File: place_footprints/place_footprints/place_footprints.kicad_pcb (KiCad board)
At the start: 2 copper layers, 64 parts

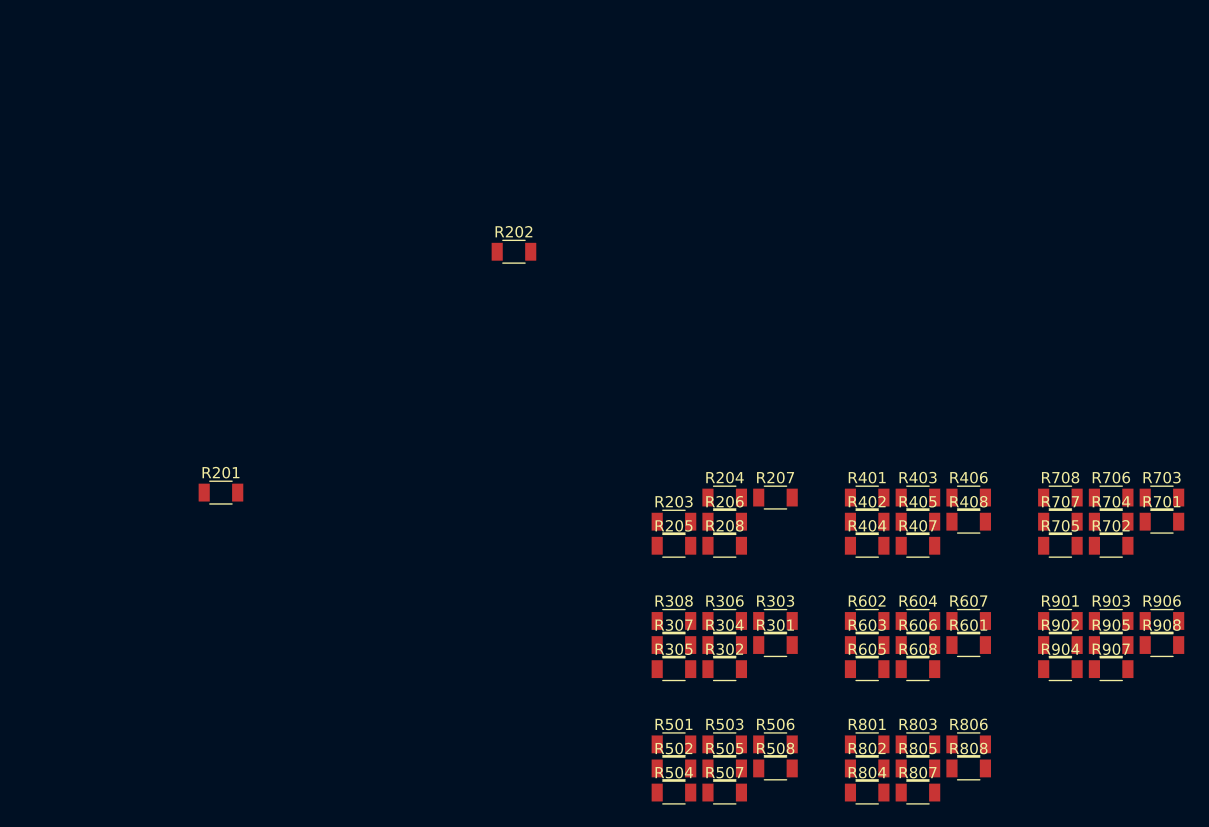
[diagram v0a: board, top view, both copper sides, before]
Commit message: Fixed circular placement
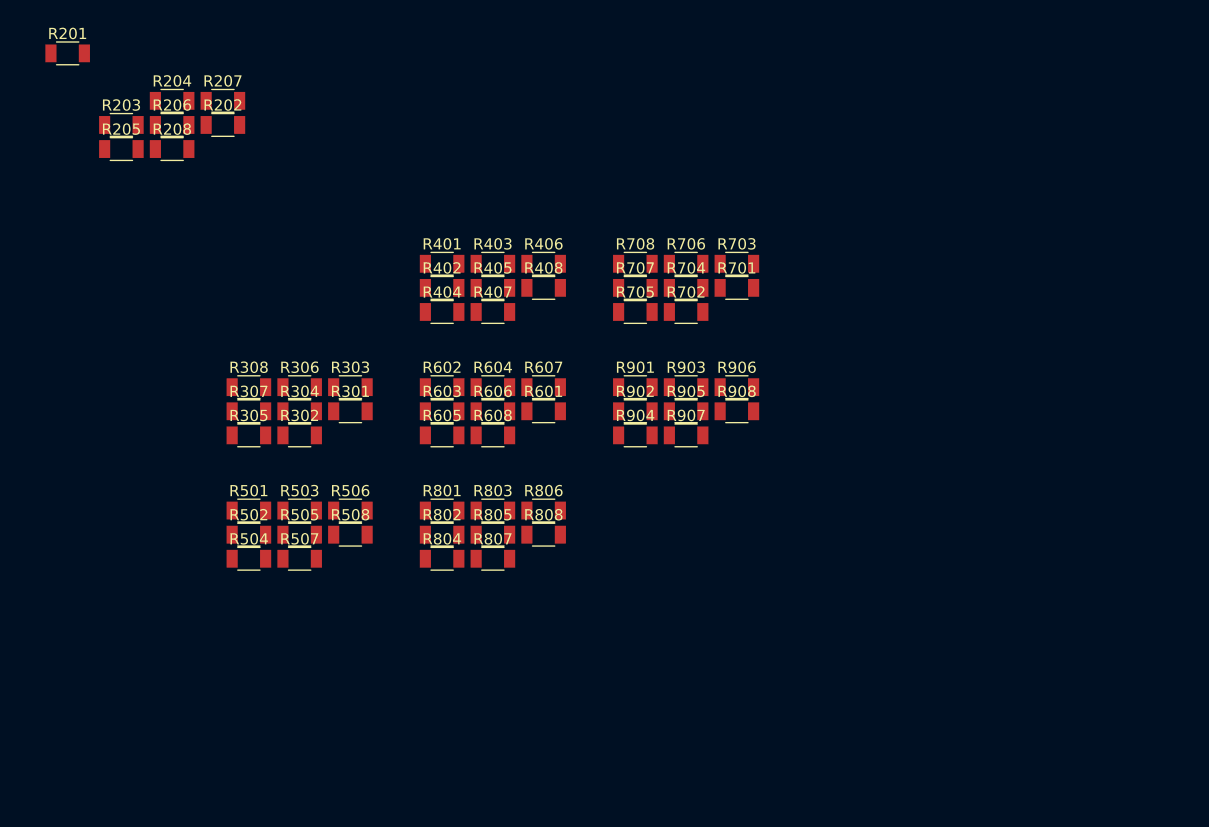
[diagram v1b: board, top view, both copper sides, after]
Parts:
- moved R204 61.0 mm to (53.2, 33.5)
- moved R206 61.0 mm to (53.2, 35.6)
- moved R208 61.0 mm to (53.2, 37.8)
- moved R207 61.0 mm to (57.7, 33.5)
- moved R203 61.0 mm to (48.6, 35.6)
- moved R205 61.0 mm to (48.6, 37.8)
- moved R301 43.5 mm to (69.2, 61.3)
- moved R302 43.5 mm to (64.6, 63.5)
- moved R303 43.5 mm to (69.2, 59.1)
- moved R304 43.5 mm to (64.6, 61.3)
- moved R306 43.5 mm to (64.6, 59.1)
- moved R401 43.5 mm to (77.4, 48.1)
- moved R402 43.5 mm to (77.4, 50.2)
- moved R404 43.5 mm to (77.4, 52.4)
- moved R503 43.5 mm to (64.6, 70.2)
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
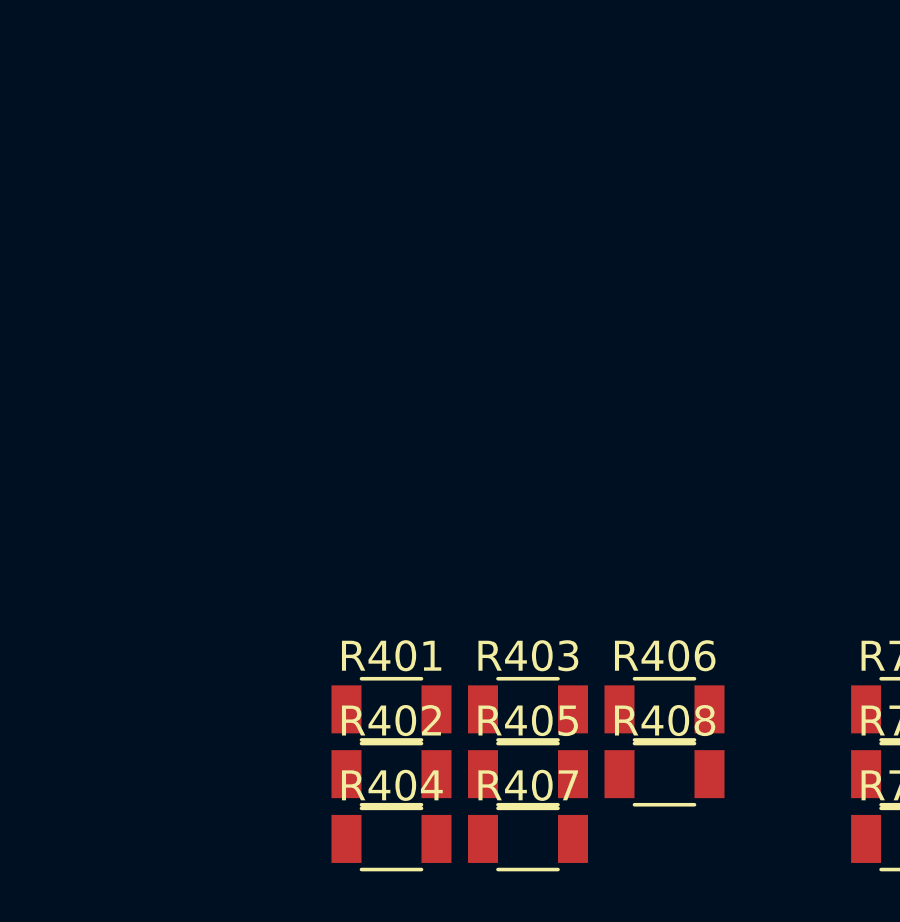
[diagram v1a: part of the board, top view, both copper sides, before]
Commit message: added support for any footprint to serve as a reference in linear and circular mode
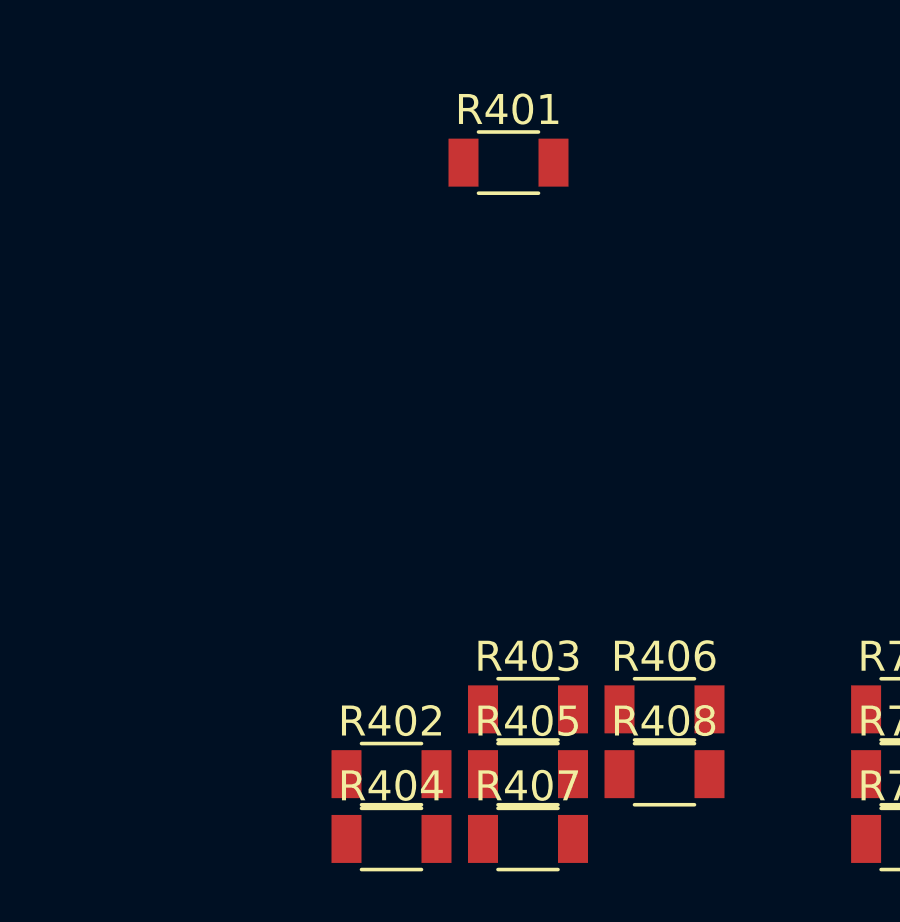
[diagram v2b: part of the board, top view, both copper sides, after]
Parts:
- moved R401 18.6 mm to (81.3, 29.8)
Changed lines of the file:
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@@
-(kicad_pcb (version 20171130) (host pcbnew "(5.0.2)-1")
+(kicad_pcb (version 20171130) (host pcbnew "(5.1.0)-1")
   (general
     (thickness 1.6)
@@
     (zone_45_only no)
     (trace_min 0.2)
-    (segment_width 0.2)
-    (edge_width 0.15)
     (via_size 0.8)
     (via_drill 0.4)
@@
     (uvia_min_size 0.2)
     (uvia_min_drill 0.1)
+    (edge_width 0.15)
+    (segment_width 0.2)
     (pcb_text_width 0.3)
     (pcb_text_size 1.5 1.5)
@@
   )
   (module Passives:R1206M (layer F.Cu)
-    (at 77.380001 48.070001)
-    (descr "Capacitor SMD 1206, reflow soldering, AVX (see smccp.pdf)")
-    (tags "capacitor 1206")
+    (at 81.28 29.845)
+    (descr "Capacitor SMD 1206, reflow soldering, AVX (see smccp.pdf)")
+    (tags "capacitor 1206")

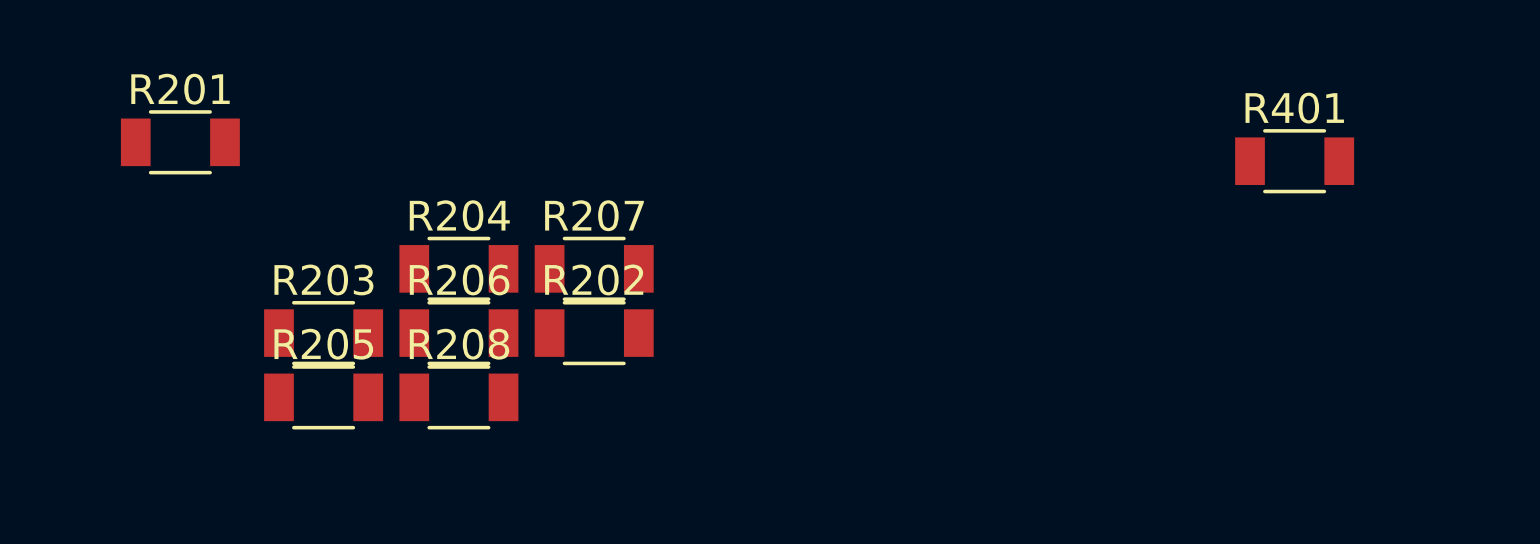
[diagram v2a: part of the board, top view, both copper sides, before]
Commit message: updated test cases
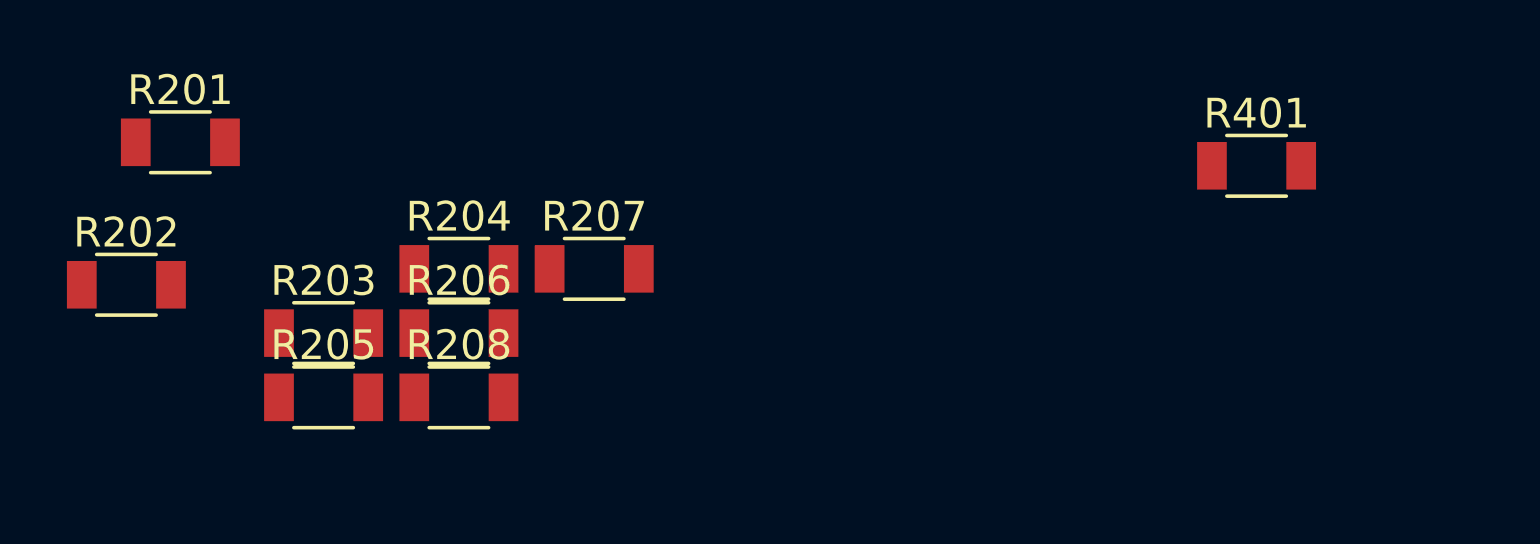
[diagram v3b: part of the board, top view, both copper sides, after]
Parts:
- moved R202 15.8 mm to (42.0, 34.0)
- moved R401 1.29 mm to (80.0, 30.0)
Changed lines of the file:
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@@
-(kicad_pcb (version 20171130) (host pcbnew "(5.1.0)-1")
+(kicad_pcb (version 20171130) (host pcbnew "(5.1.5-90-g5c7ac1bb7)-1")
   (general
     (thickness 1.6)
@@
   )
   (module Passives:R1206M (layer F.Cu)
-    (at 57.730001 35.625001)
+    (at 42 34)
     (descr "Capacitor SMD 1206, reflow soldering, AVX (see smccp.pdf)")
     (tags "capacitor 1206")
@@
   )
   (module Passives:R1206M (layer F.Cu)
-    (at 81.28 29.845)
-    (descr "Capacitor SMD 1206, reflow soldering, AVX (see smccp.pdf)")
-    (tags "capacitor 1206")
+    (at 80 30)
+    (descr "Capacitor SMD 1206, reflow soldering, AVX (see smccp.pdf)")
+    (tags "capacitor 1206")
